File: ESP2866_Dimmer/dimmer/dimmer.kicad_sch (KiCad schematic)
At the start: 17 parts, among them J1 Conn_01x04_Male, J2 Screw_Terminal_01x03, J4 Screw_Terminal_01x02, J7 Screw_Terminal_01x02, K1 HF46F/12-HS1, Q1 2N3904

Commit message: Додано документацію на Wifi модуль реле. Оновлена схема та бібліотека.
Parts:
- removed D1: 1N4007, Diode_THT:D_DO-41_SOD81_P5.08mm_Vertical_AnodeUp, symbol Diode:1N4007
- removed K1: HF46F/12-HS1, cnc_pump:HF46F12-HS1, symbol cnc_pump:HF46F12-HS1
- removed Q1: 2N3904, Package_TO_SOT_THT:TO-92_Inline, symbol Transistor_BJT:2N3904
- removed R4: 10к, Resistor_THT:R_Axial_DIN0207_L6.3mm_D2.5mm_P10.16mm_Horizontal, symbol Device:R
- added CR? (x3): SMBJ6.5CA, SMBJSeries_LTF, symbol dimmer_lib:SMBJ6.5CA
- added J?: Screw_Terminal_01x04, symbol Connector:Screw_Terminal_01x04
- added R? (x3): 1k, Resistor_THT:R_Axial_DIN0207_L6.3mm_D2.5mm_P10.16mm_Horizontal, symbol Device:R
- added R? (x3): 4.7k, Resistor_THT:R_Axial_DIN0207_L6.3mm_D2.5mm_P10.16mm_Horizontal, symbol Device:R
- added R?: 10k, Resistor_THT:R_Axial_DIN0207_L6.3mm_D2.5mm_P10.16mm_Horizontal, symbol Device:R
- added R?: 0, Resistor_THT:R_Axial_DIN0207_L6.3mm_D2.5mm_P10.16mm_Horizontal, symbol Device:R
- added U? (x3): LTV-817, Package_DIP:DIP-4_W7.62mm, symbol Isolator:LTV-817
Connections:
- net +3V3: now also R?.1, R?.1, R?.1, R?.1, R?.2; no longer C4.1, U?.4 (Vo)
- net GND: now also R?.2, U?.3, U?.3, U?.3
- net GNDPWR: now also CR?.2, CR?.2, CR?.2, J?.4 (Pin_4), U?.2, U?.2, U?.2
- net ON_OFF: now reaches U?.12 (GPIO10)
- net ON_OFF: now also R?.2, U?.4
- net UP: now reaches U?.13 (MOSI)
- net UP: now also R?.2, U?.4
- net DOWN: now reaches U?.14 (SCLK)
- net DOWN: now also R?.2, U?.4
- net MOVE_SENSOR: now reaches U?.20 (GPIO5)
- net PWM: now reaches U?.4 (GPIO16)
- new net: C4.1, R?.1, U?.4 (Vo)
- new net: CR?.1, J?.3 (Pin_3), R?.1
- new net: R?.2, U?.1 (x3)
- new net: CR?.1, J?.2 (Pin_2), R?.1
- new net: CR?.1, J?.1 (Pin_1), R?.1

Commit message: Оновлення схеми.
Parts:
- removed J2: Screw_Terminal_01x03, cnc_pump:CON1x3p5mm, symbol Connector:Screw_Terminal_01x03
- removed J4: Screw_Terminal_01x02, cnc_pump:CON1x2p5mm, symbol Connector:Screw_Terminal_01x02
- added J?: Conn_01x03_Male, Connector_JST:JST_EH_B3B-EH-A_1x03_P2.50mm_Vertical, symbol Connector:Conn_01x03_Male
- added J?: Conn_01x03_Male, symbol Connector:Conn_01x03_Male
- added K?: IM43, symbol Relay:IM43
- added R?: 4.7k, Resistor_THT:R_Axial_DIN0207_L6.3mm_D2.5mm_P10.16mm_Horizontal, symbol Device:R
- added SW?: SW_Push, symbol Switch:SW_Push
- added U?: LTV-817, Package_DIP:DIP-4_W7.62mm, symbol Isolator:LTV-817
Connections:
- net +3V3: now also J?.1 (Pin_1), J?.1 (Pin_1)
- net +5V: now also K?.1
- net DOWN: now also U?.5 (GPIO14); no longer U?.14 (SCLK)
- net GND: now also J?.3 (Pin_3), J?.3 (Pin_3), SW?.1, U?.2
- net GNDPWR: now also U?.3
- net LIGHT_SENSOR: now also U?.6 (GPIO12), J?.2 (Pin_2)
- net MOVE_SENSOR: now also J?.2 (Pin_2)
- net PWM: now also U?.19 (GPIO4); no longer U?.4 (GPIO16)
- net UP: now also U?.7 (GPIO13); no longer U?.13 (MOSI)
- net at R2.2, U?.1 (~{RST}): now also SW?.2
- new net: K?.8, U?.4
- new net: R?.2, U?.1
- new net LED_ON_RELE: R?.1
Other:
- moved on the sheet: R1, R2, U?

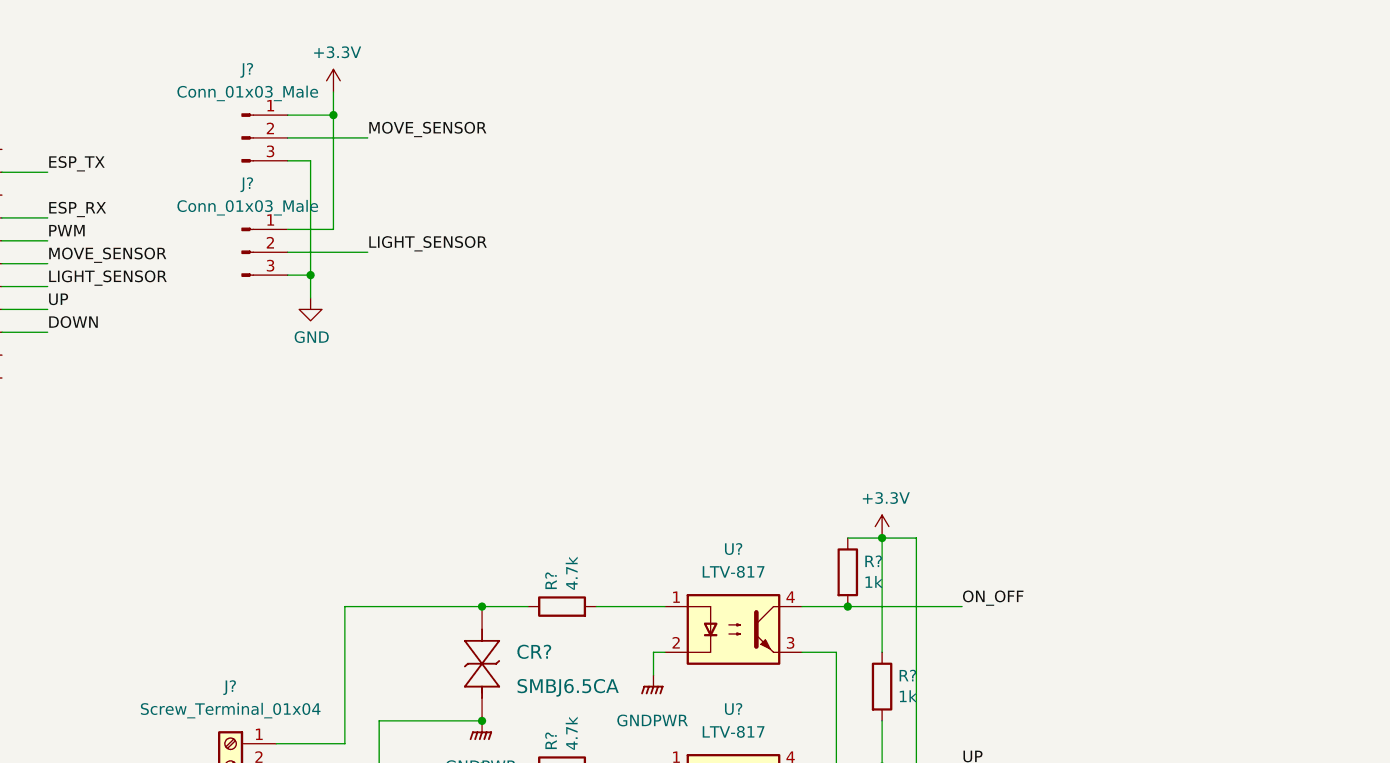
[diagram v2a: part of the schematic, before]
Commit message: Додав символ LED драйвера LDH-45A-350. Оновив схему.
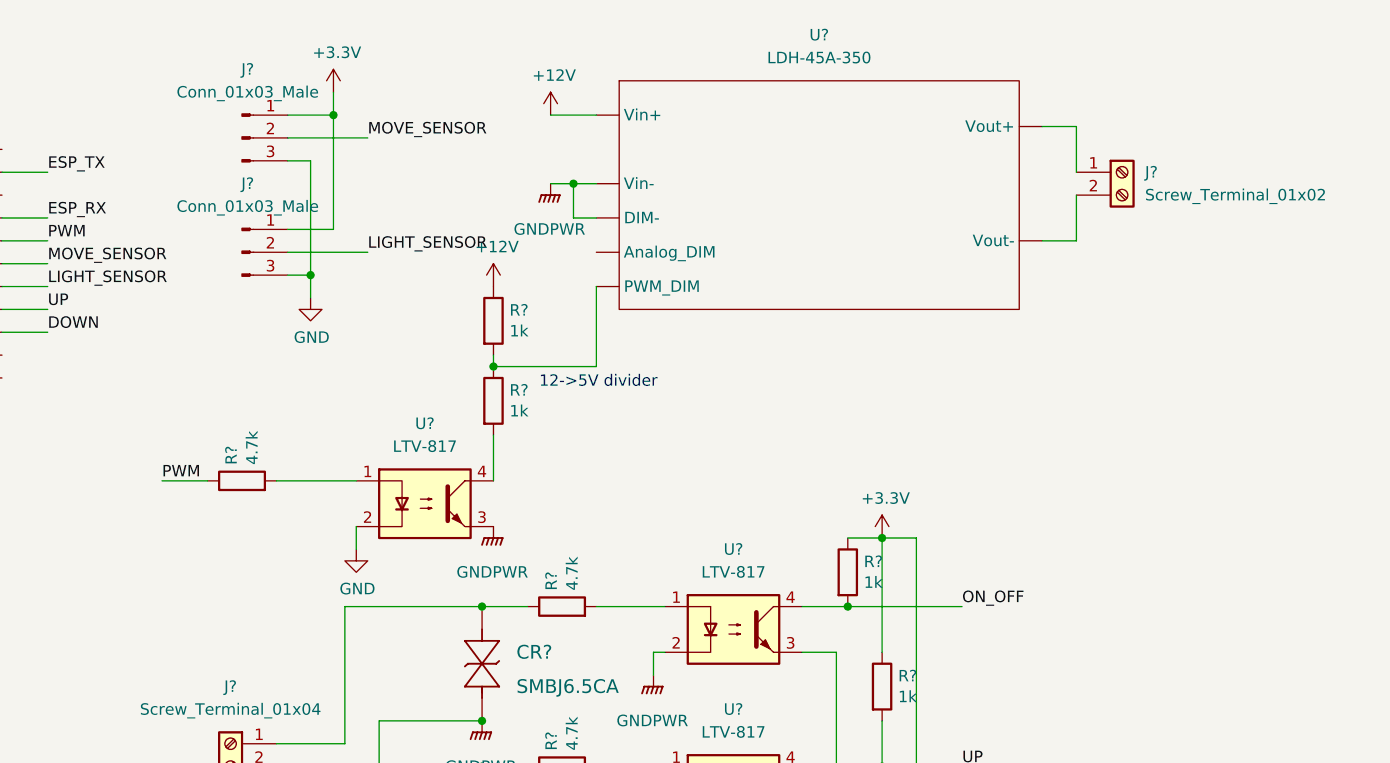
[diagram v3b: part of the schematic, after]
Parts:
- added J?: Screw_Terminal_01x02, symbol Connector:Screw_Terminal_01x02
- added R? (x2): 1k, Resistor_THT:R_Axial_DIN0207_L6.3mm_D2.5mm_P10.16mm_Horizontal, symbol Device:R
- added R?: 4.7k, Resistor_THT:R_Axial_DIN0207_L6.3mm_D2.5mm_P10.16mm_Horizontal, symbol Device:R
- added U?: LTV-817, Package_DIP:DIP-4_W7.62mm, symbol Isolator:LTV-817
- added U?: LDH-45A-350, symbol dimmer_lib:LDH-45A-350
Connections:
- net +12V: now also R?.1, U?. (Vout-)
- net GND: now also U?.2
- net GNDPWR: now also U?. (Vout-), U?.3
- net PWM: now also R?.1
- new net: J?.1 (Pin_1), U?. (Vout-)
- new net: J?.2 (Pin_2), U?. (Vout-)
- new net: R?.2, U?.1
- new net: R?.2, U?.4
- new net: R?.1, R?.2, U?. (Vout-)
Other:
- note added: "12->5V divider"

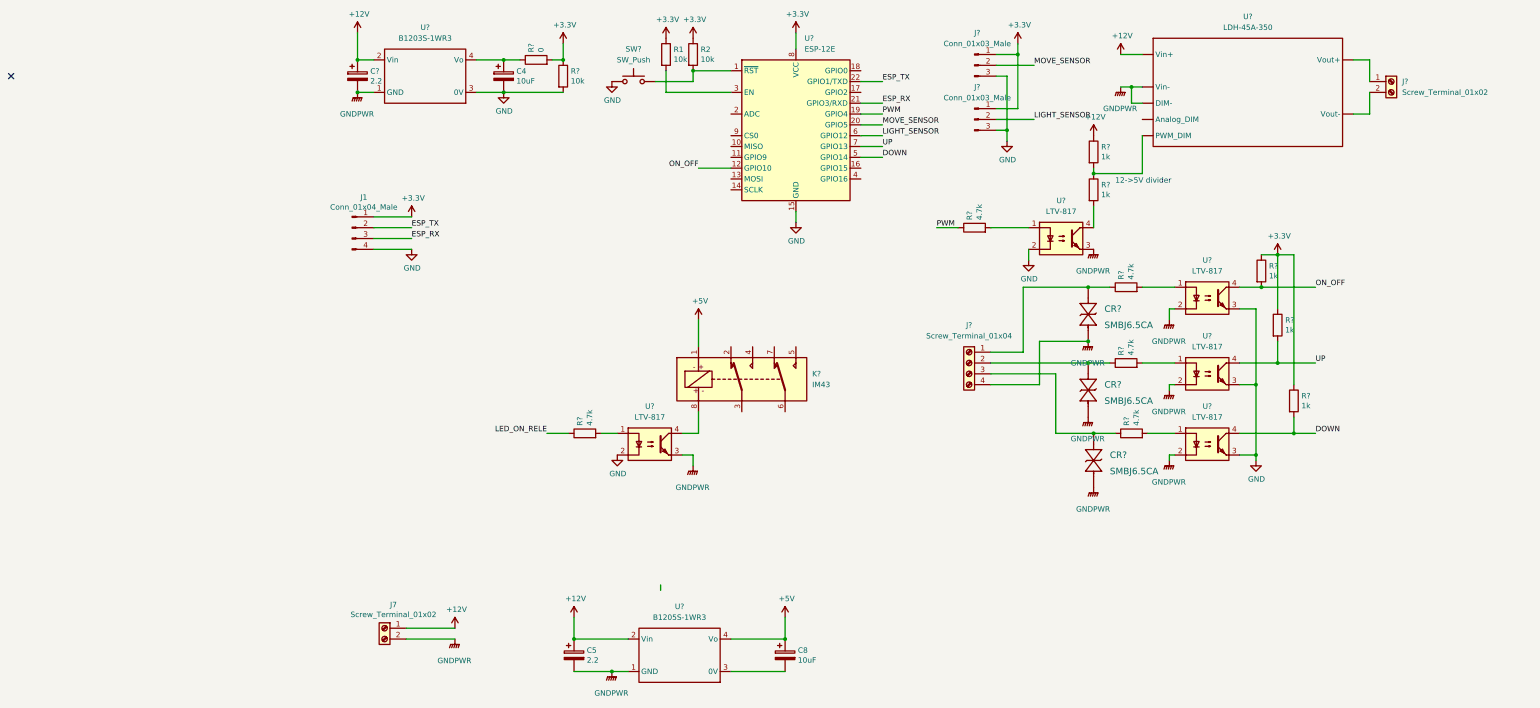
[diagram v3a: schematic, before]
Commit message: Оновлення схеми. Зміна типу оптрону.
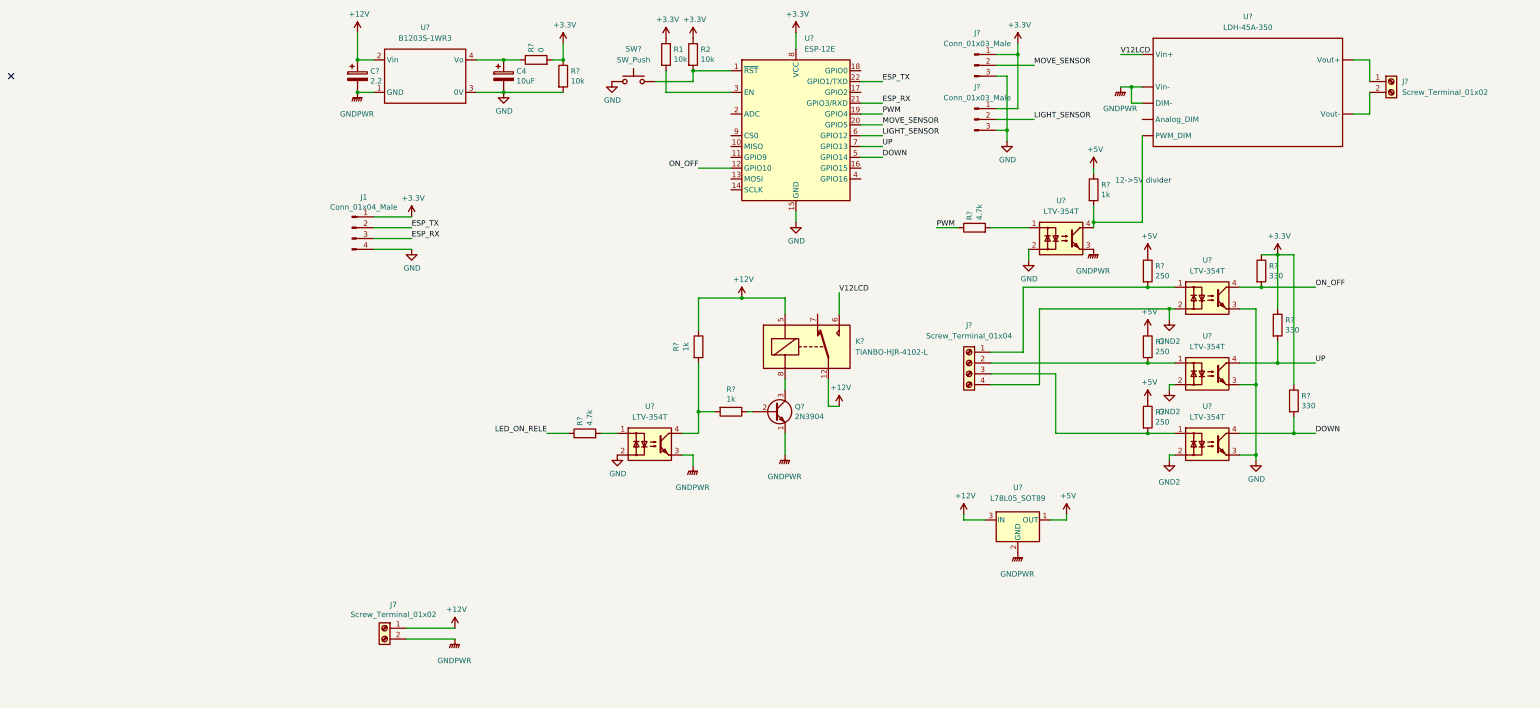
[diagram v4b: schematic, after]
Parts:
- removed C5: 2.2, Capacitor_THT:CP_Radial_D5.0mm_P2.50mm, symbol Device:CP
- removed C8: 10uF, Capacitor_THT:CP_Radial_D5.0mm_P2.00mm, symbol Device:CP
- removed CR? (x3): SMBJ6.5CA, SMBJSeries_LTF, symbol dimmer_lib:SMBJ6.5CA
- removed K?: IM43, symbol Relay:IM43
- removed R?: 1k, Resistor_THT:R_Axial_DIN0207_L6.3mm_D2.5mm_P10.16mm_Horizontal, symbol Device:R
- removed U? (x5): LTV-817, Package_DIP:DIP-4_W7.62mm, symbol Isolator:LTV-817
- removed U?: B1205S-1WR3, symbol dimmer_lib:B1205S-1WR3
- added K?: TIANBO-HJR-4102-L, Relay_THT:Relay_SPDT_HJR-4102, symbol Relay:TIANBO-HJR-4102-L
- added Q?: 2N3904, Package_TO_SOT_THT:TO-92_Inline, symbol Transistor_BJT:2N3904
- added R? (x2): 1k, Resistor_THT:R_Axial_DIN0207_L6.3mm_D2.5mm_P10.16mm_Horizontal, symbol Device:R
- added U? (x5): LTV-354T, Package_SO:SO-4_4.4x3.6mm_P2.54mm, symbol Isolator:LTV-354T
- added U?: L78L05_SOT89, Package_TO_SOT_SMD:SOT-89-3, symbol Regulator_Linear:L78L05_SOT89
- R? (x3): value 1k -> 330
- R? (x3): value 4.7k -> 250
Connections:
- net +12V: now also K?.12, K?.5, R?.1, U?.3 (IN); no longer U?. (Vout-)
- net +5V: now also R?.1, R?.1, R?.1, R?.1, U?.1 (OUT)
- net DOWN: now also U?.4
- net GND: now also U?.2, U?.2, U?.3, U?.3, U?.3
- net GNDPWR: now also Q?.1 (E), U?.2 (GND), U?.3, U?.3; no longer J?.4 (Pin_4)
- net ON_OFF: now also U?.4
- net UP: now also U?.4
- net at J?.3 (Pin_3): now also R?.2, U?.1; no longer R?.1
- net at R?.2: now also J?.1 (Pin_1), U?.1
- net at R?.2: now also J?.2 (Pin_2), U?.1
- net at R?.2: now also U?.1 (x2)
- net at R?.2: now also U?. (Vout-), U?.4
- net V12LCD: now reaches U?. (Vout-)
- net V12LCD: now also K?.6; no longer R?.1
- new net: Q?.2 (B), R?.1
- new net: R?.2, R?.2, U?.4
- new net: K?.8, Q?.3 (C)
- new net GND2: J?.4 (Pin_4), U?.2, U?.2, U?.2
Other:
- moved on the sheet: R?

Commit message: Фінальний варіант схеми. Початковий варінт друкованної плати.
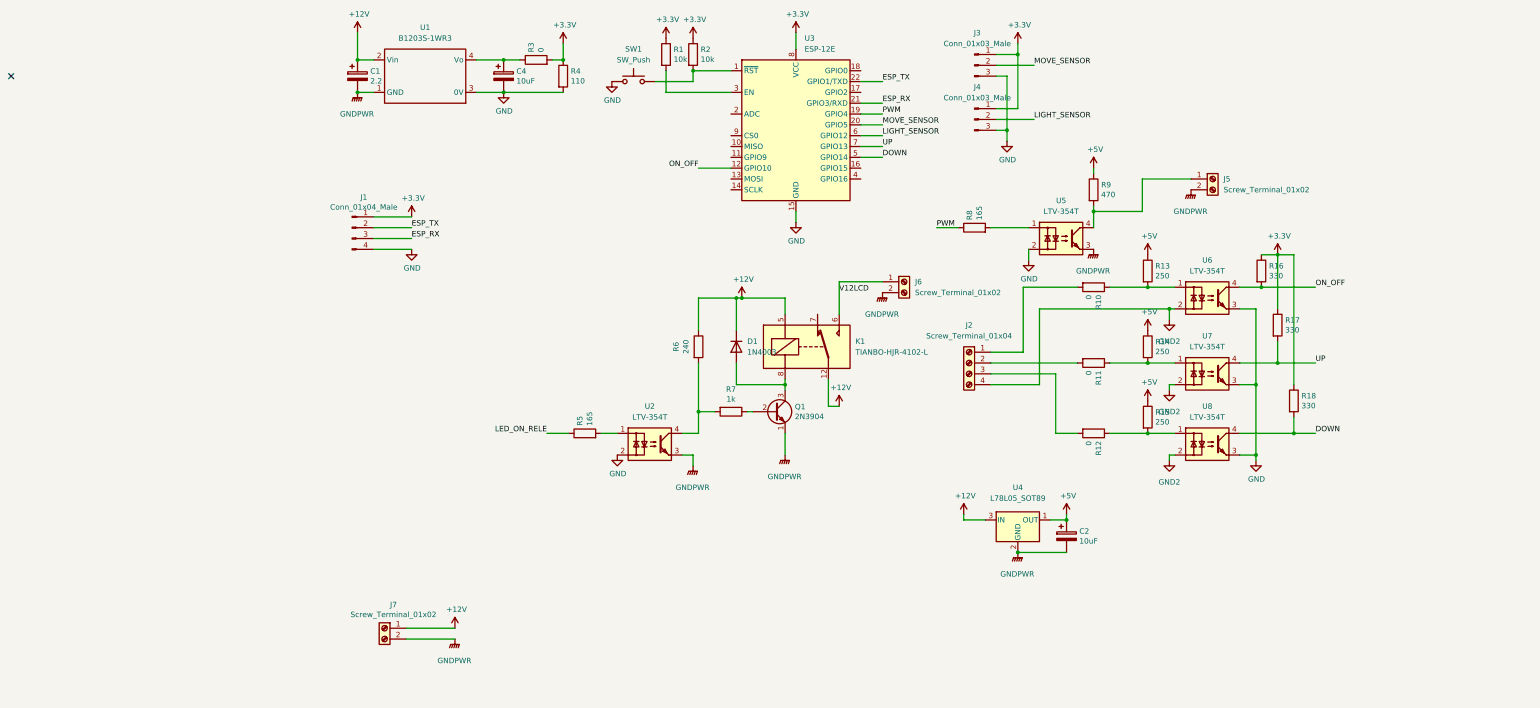
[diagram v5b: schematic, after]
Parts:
- removed U?: LDH-45A-350, symbol dimmer_lib:LDH-45A-350
- added C2: 10uF, Capacitor_SMD:CP_Elec_4x5.3, symbol Device:CP
- added D1: 1N4003, Diode_SMD:D_SMA, symbol Diode:1N4003
- added J5: Screw_Terminal_01x02, Connector_JST:JST_NV_B02P-NV_1x02_P5.00mm_Vertical, symbol Connector:Screw_Terminal_01x02
- added R10, R11, R12: 0, Resistor_SMD:R_1206_3216Metric_Pad1.30x1.75mm_HandSolder, symbol Device:R
- C1: renamed from C?; footprint Capacitor_THT:CP_Radial_D5.0mm_P2.50mm -> Capacitor_SMD:CP_Elec_4x5.3
- C4: footprint Capacitor_THT:CP_Radial_D5.0mm_P2.50mm -> Capacitor_SMD:CP_Elec_4x5.3
- J2: renamed from J?; footprint (none) -> Connector_JST:JST_NV_B04P-NV_1x04_P5.00mm_Vertical
- J6: renamed from J?; footprint (none) -> Connector_JST:JST_NV_B02P-NV_1x02_P5.00mm_Vertical
- J7: footprint cnc_pump:CON1x2p5mm -> Connector_JST:JST_NV_B02P-NV_1x02_P5.00mm_Vertical
- R1, R2: footprint Resistor_THT:R_Axial_DIN0207_L6.3mm_D2.5mm_P10.16mm_Horizontal -> Resistor_SMD:R_1206_3216Metric_Pad1.30x1.75mm_HandSolder
- R13, R14, R15, R16, R17, R18, R3, R7: renamed from R?; footprint Resistor_THT:R_Axial_DIN0207_L6.3mm_D2.5mm_P10.16mm_Horizontal -> Resistor_SMD:R_1206_3216Metric_Pad1.30x1.75mm_HandSolder
- R4: renamed from R?; value 10k -> 110; footprint Resistor_THT:R_Axial_DIN0207_L6.3mm_D2.5mm_P10.16mm_Horizontal -> Resistor_SMD:R_1206_3216Metric_Pad1.30x1.75mm_HandSolder
- R5, R8: renamed from R?; value 4.7k -> 165; footprint Resistor_THT:R_Axial_DIN0207_L6.3mm_D2.5mm_P10.16mm_Horizontal -> Resistor_SMD:R_1206_3216Metric_Pad1.30x1.75mm_HandSolder
- R6: renamed from R?; value 1k -> 240; footprint Resistor_THT:R_Axial_DIN0207_L6.3mm_D2.5mm_P10.16mm_Horizontal -> Resistor_SMD:R_1206_3216Metric_Pad1.30x1.75mm_HandSolder
- R9: renamed from R?; value 1k -> 470; footprint Resistor_THT:R_Axial_DIN0207_L6.3mm_D2.5mm_P10.16mm_Horizontal -> Resistor_SMD:R_1206_3216Metric_Pad1.30x1.75mm_HandSolder
- SW1: renamed from SW?; footprint (none) -> Button_Switch_SMD:SW_DIP_SPSTx01_Slide_6.7x4.1mm_W6.73mm_P2.54mm_LowProfile_JPin
- gave numbers to parts that had none: 12
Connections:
- net +12V: now also D1.1 (K)
- net +5V: now also C2.1
- net GNDPWR: now also J6.2 (Pin_2), C2.2, J5.2 (Pin_2)
- net V12LCD: now also J6.1 (Pin_1)
- net at R14.2, U7.1: now also R11.1; no longer J2.2 (Pin_2)
- net at R13.2, U6.1: now also R10.1; no longer J2.1 (Pin_1)
- net at R15.2, U8.1: now also R12.1; no longer J2.3 (Pin_3)
- net at R9.2, U5.4: now also J5.1 (Pin_1)
- net at K1.8, Q1.3 (C): now also D1.2 (A)
- new net: J2.1 (Pin_1), R10.2
- new net: J2.2 (Pin_2), R11.2
- new net: J2.3 (Pin_3), R12.2
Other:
- note removed: "12->5V divider"
- moved on the sheet: J6

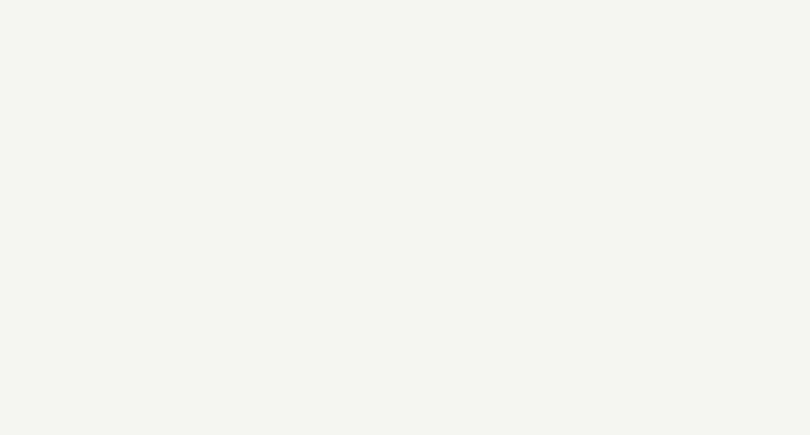
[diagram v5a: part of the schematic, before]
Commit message: Оновлення схеми. Додано 3Д модель перетворювача.
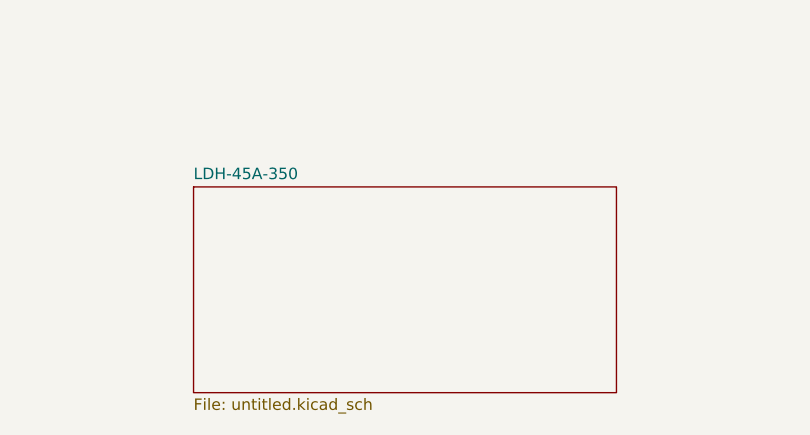
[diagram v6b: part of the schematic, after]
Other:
- added sheet LDH-45A-350 (untitled.kicad_sch)
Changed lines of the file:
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@@
     (pin "1")
+  )
+  (sheet (at 95.25 151.13) (size 46.99 22.86) (fields_autoplaced)
+    (stroke (width 0.1524) (type solid) (color 0 0 0 0))
+    (fill (color 0 0 0 0.0000))
+    (property "Sheet name" "LDH-45A-350" (id 0) (at 95.25 150.4184 0)
+      (effects (font (size 1.27 1.27)) (justify left bottom))
+    )
+    (property "Sheet file" "untitled.kicad_sch" (id 1) (at 95.25 174.5746 0)
+      (effects (font (size 1.27 1.27)) (justify left top))
+    )
   )
   (sheet_instances
     (path "/" (page "1"))
+    (path "/f8371471-4211-4368-9dd3-157e5ded70c0" (page "2"))
   )
   (symbol_instances
@@
       (reference "J7") (unit 1) (value "Screw_Terminal_01x02") (footprint "Connector_JST:JST_NV_B02P-NV_1x02_P5.00mm_Vertical")
     )
+    (path "/f8371471-4211-4368-9dd3-157e5ded70c0/60e7850f-d81d-4b57-a82d-002416a7a2a2"
+      (reference "J?") (unit 1) (value "Conn_01x04_Male") (footprint "")
+    )
+    (path "/f8371471-4211-4368-9dd3-157e5ded70c0/7b7b0a39-4c5a-4b75-b108-79e2ffeb37c7"
+      (reference "J?") (unit 1) (value "Conn_01x04_Male") (footprint "")
+    )
+    (path "/f8371471-4211-4368-9dd3-157e5ded70c0/8defd7fa-4f3e-463e-80fe-a61c4cda154a"
+      (reference "J?") (unit 1) (value "Conn_01x04_Male") (footprint "")
+    )
     (path "/dcc8b3c7-e00a-4c96-92c3-7cf68574fa70"
       (reference "K1") (unit 1) (value "TIANBO-HJR-4102-L") (footprint "Relay_THT:Relay_SPDT_HJR-4102")
@@
       (reference "U8") (unit 1) (value "LTV-354T") (footprint "Package_SO:SO-4_4.4x3.6mm_P2.54mm")
     )
-  )
+    (path "/f8371471-4211-4368-9dd3-157e5ded70c0/464aa031-265c-410d-83c1-58d5ac5e6c8d"
+      (reference "U?") (unit 1) (value "LDH-45A-350") (footprint "")
+    )
+  )
